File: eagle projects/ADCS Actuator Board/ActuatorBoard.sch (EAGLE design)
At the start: 228 parts, among them J11 TE_1-84953-1, J2 TE_1-84953-1, J4 TE_1-84953-1, J5 TE-1734829-3, U1 SIP2100DY-T1-GE3, U10 LM2917MX/NOPB, U12 TSV991AILT, U13 LM2917MX/NOPB, U14 ADS7841E_2K5, U16 DRV10970_MOTOR_DRIVERDRV10970, U17 LM2917MX/NOPB, U19 TSV991AILT, U2 SIP2100DY-T1-GE3, U20 ADS7841E_2K5, U3 SIP2100DY-T1-GE3, U6 DRV10970_MOTOR_DRIVERDRV10970, U7 DRV10970_MOTOR_DRIVERDRV10970, U8 TSV991AILT, U9 ADS7841E_2K5

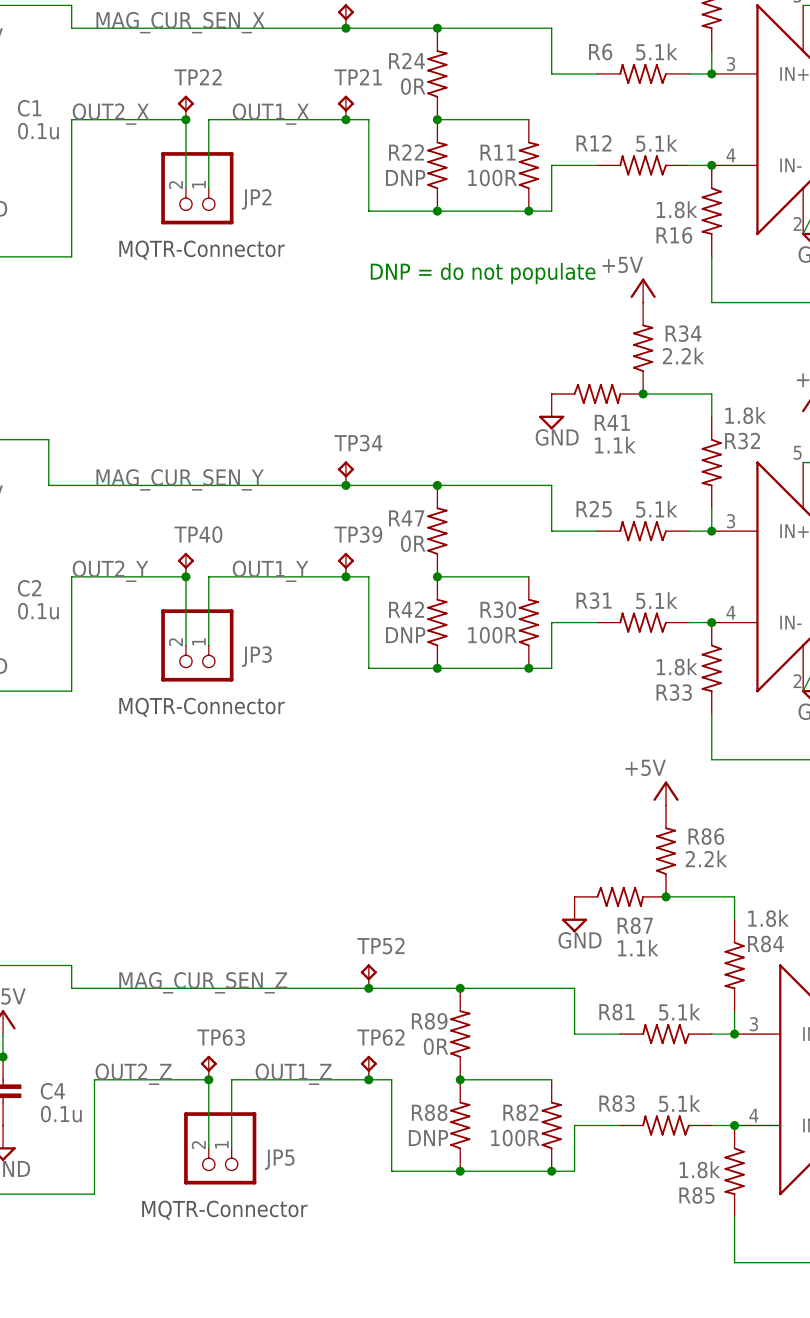
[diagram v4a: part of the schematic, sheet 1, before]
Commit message: Updated Actuator board BOM and populated necessary resistors on Z+ board
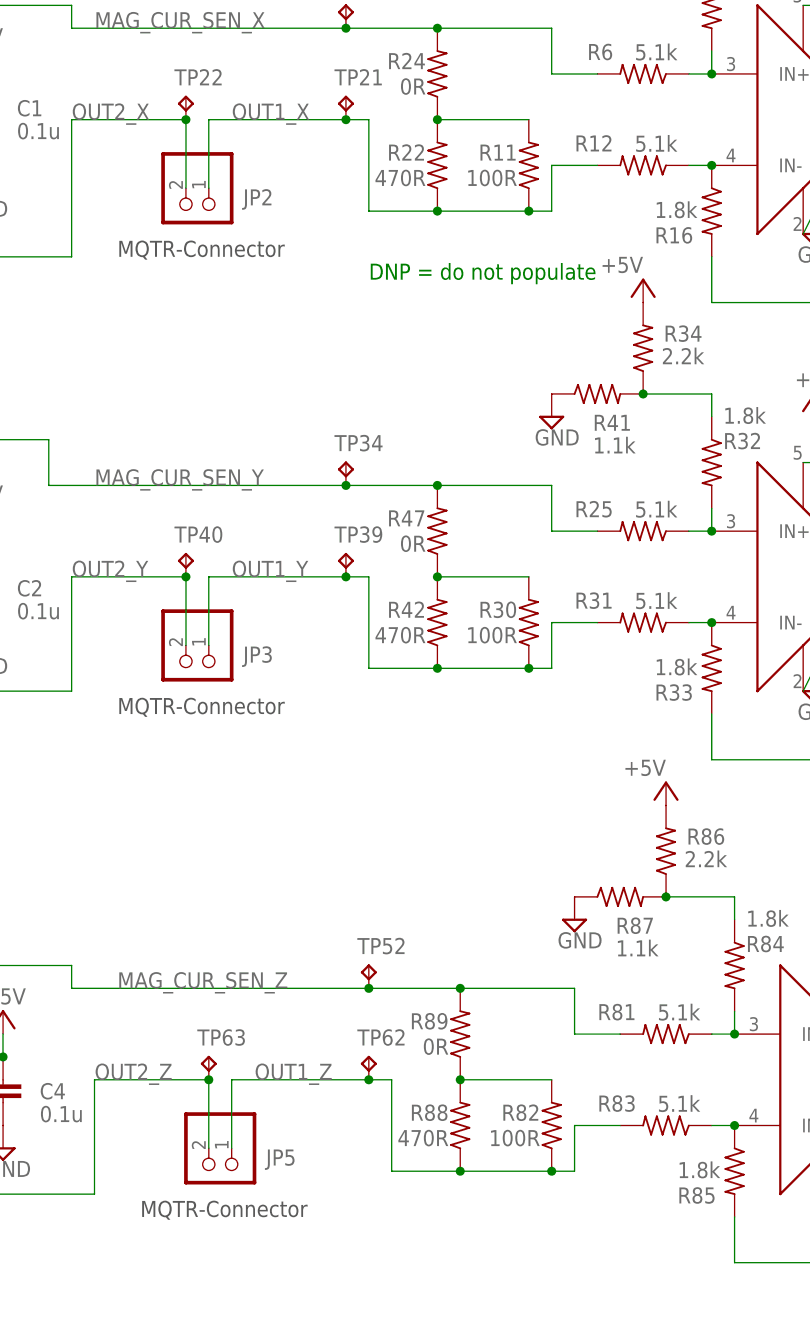
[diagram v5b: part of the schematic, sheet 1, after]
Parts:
- R22, R42, R88: value DNP -> 470R
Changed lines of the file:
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@@
 <part name="P+11" library="supply1" library_urn="urn:adsk.eagle:library:371" deviceset="+5V" device=""/>
 <part name="JP2" library="pinhead" library_urn="urn:adsk.eagle:library:325" deviceset="PINHD-1X2" device="" package3d_urn="urn:adsk.eagle:package:22435/2"/>
-<part name="R22" library="rcl" library_urn="urn:adsk.eagle:library:334" deviceset="R-US_" device="R0805" package3d_urn="urn:adsk.eagle:package:23553/2" value="DNP"/>
+<part name="R22" library="rcl" library_urn="urn:adsk.eagle:library:334" deviceset="R-US_" device="R0805" package3d_urn="urn:adsk.eagle:package:23553/2" value="470R"/>
 <part name="R24" library="rcl" library_urn="urn:adsk.eagle:library:334" deviceset="R-US_" device="R0805" package3d_urn="urn:adsk.eagle:package:23553/2" value="0R"/>
 <part name="TP17" library="my_library" library_urn="urn:adsk.eagle:library:22876504" deviceset="TESTPOINT" device="" package3d_urn="urn:adsk.eagle:package:24605432/3"/>
@@
 <part name="P+15" library="supply1" library_urn="urn:adsk.eagle:library:371" deviceset="+5V" device=""/>
 <part name="JP3" library="pinhead" library_urn="urn:adsk.eagle:library:325" deviceset="PINHD-1X2" device="" package3d_urn="urn:adsk.eagle:package:22435/2"/>
-<part name="R42" library="rcl" library_urn="urn:adsk.eagle:library:334" deviceset="R-US_" device="R0805" package3d_urn="urn:adsk.eagle:package:23553/2" value="DNP"/>
+<part name="R42" library="rcl" library_urn="urn:adsk.eagle:library:334" deviceset="R-US_" device="R0805" package3d_urn="urn:adsk.eagle:package:23553/2" value="470R"/>
 <part name="R47" library="rcl" library_urn="urn:adsk.eagle:library:334" deviceset="R-US_" device="R0805" package3d_urn="urn:adsk.eagle:package:23553/2" value="0R"/>
 <part name="TP34" library="my_library" library_urn="urn:adsk.eagle:library:22876504" deviceset="TESTPOINT" device="" package3d_urn="urn:adsk.eagle:package:24605432/3"/>
@@
 <part name="P+24" library="supply1" library_urn="urn:adsk.eagle:library:371" deviceset="+5V" device=""/>
 <part name="JP5" library="pinhead" library_urn="urn:adsk.eagle:library:325" deviceset="PINHD-1X2" device="" package3d_urn="urn:adsk.eagle:package:22435/2"/>
-<part name="R88" library="rcl" library_urn="urn:adsk.eagle:library:334" deviceset="R-US_" device="R0805" package3d_urn="urn:adsk.eagle:package:23553/2" value="DNP"/>
+<part name="R88" library="rcl" library_urn="urn:adsk.eagle:library:334" deviceset="R-US_" device="R0805" package3d_urn="urn:adsk.eagle:package:23553/2" value="470R"/>
 <part name="R89" library="rcl" library_urn="urn:adsk.eagle:library:334" deviceset="R-US_" device="R0805" package3d_urn="urn:adsk.eagle:package:23553/2" value="0R"/>
 <part name="TP52" library="my_library" library_urn="urn:adsk.eagle:library:22876504" deviceset="TESTPOINT" device="" package3d_urn="urn:adsk.eagle:package:24605432/3"/>
